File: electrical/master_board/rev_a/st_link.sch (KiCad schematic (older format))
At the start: 1 part, among them CN90 STADAPTER;F2x4

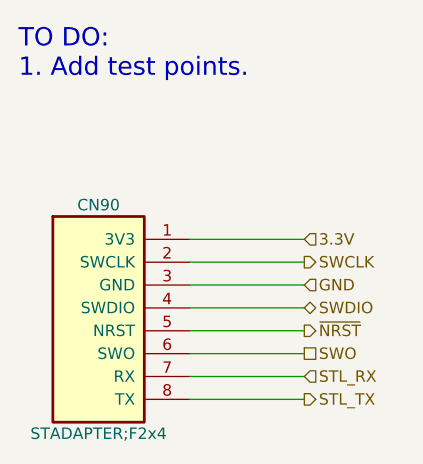
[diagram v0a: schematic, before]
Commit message: Pin reassignments to support servo current.
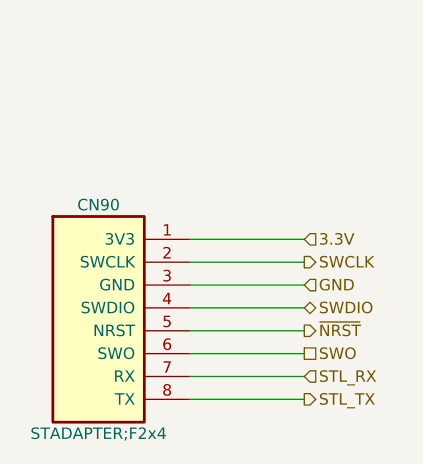
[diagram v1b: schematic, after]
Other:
- note removed: "TO DO:\n1. Add test points."
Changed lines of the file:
@@
 Wire Wire Line
 	6000 4350 6500 4350
-Text Notes 5250 2950 0    80   ~ 0
-TO DO:\n1. Add test points.
 $EndSCHEMATC

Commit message: More work thinning rats nest of unconnected wires.
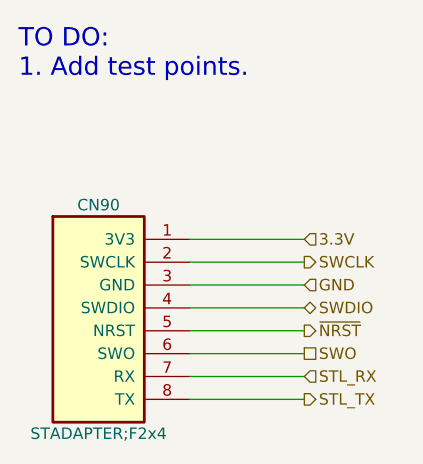
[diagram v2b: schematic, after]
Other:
- note added: "TO DO:\n1. Add test points."
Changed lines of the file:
@@
 Wire Wire Line
 	6000 4350 6500 4350
+Text Notes 5250 2950 0    80   ~ 0
+TO DO:\n1. Add test points.
 $EndSCHEMATC
